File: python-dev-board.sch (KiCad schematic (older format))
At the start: 36 parts, among them IC1 STM32F405RGT, J1 Conn_01x17, J2 Conn_01x17, J3 USB_OTG, J4 47309-2851, SW1 SW_Push, U1 LM1117-3.3, Y1 8MHz, Y2 32.768KHz

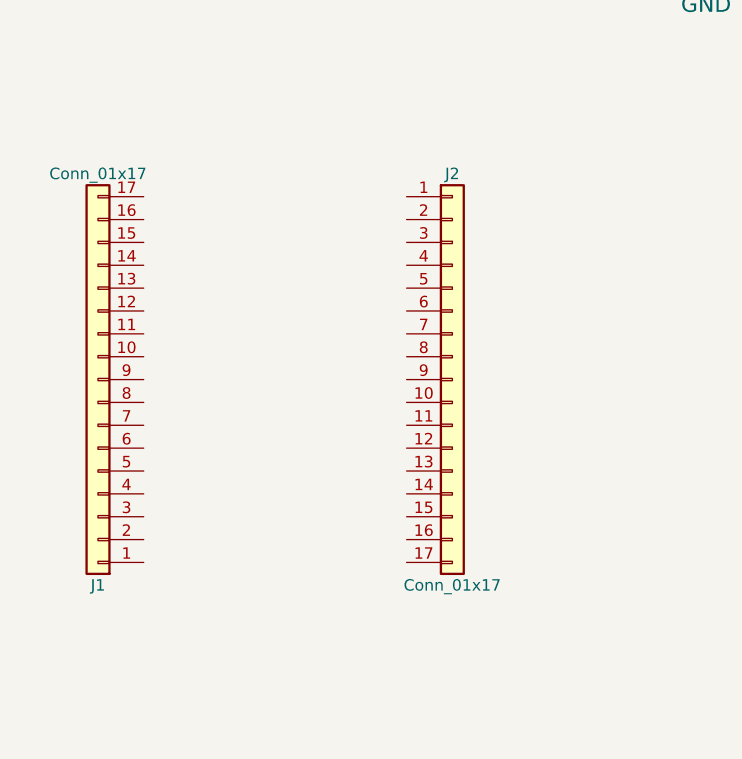
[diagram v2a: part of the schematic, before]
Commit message: connected gpio to pin header
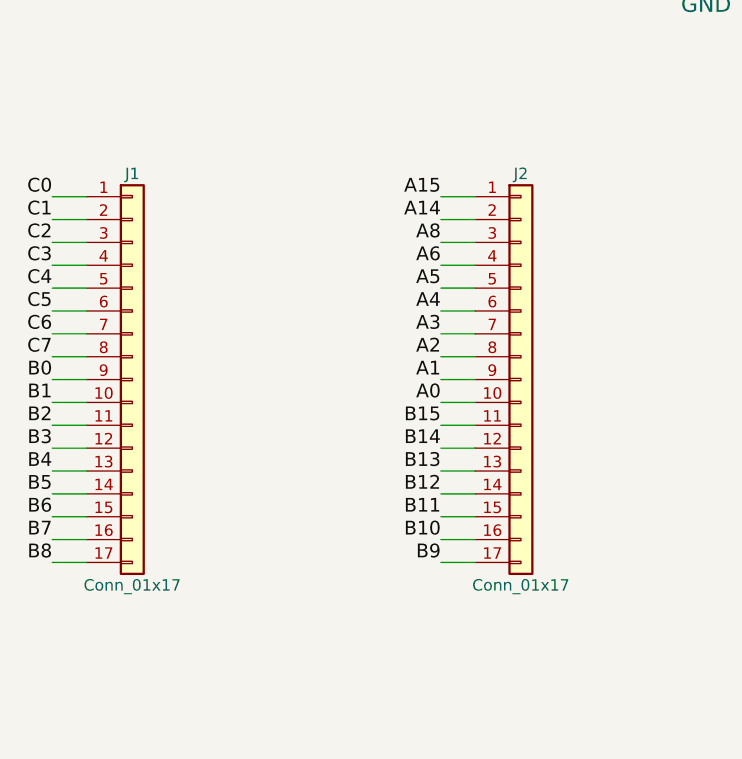
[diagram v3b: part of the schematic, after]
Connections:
- wire segments 154 -> 188
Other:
- moved on the sheet: J2
